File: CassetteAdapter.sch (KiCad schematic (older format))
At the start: 20 parts, among them CN1 AUDIO_IN, CN101 AUDIO_IN_JACK, CN2 TAPE_PORT, SW1 SW_INVERT1, U1 CD4049, U2 LM741

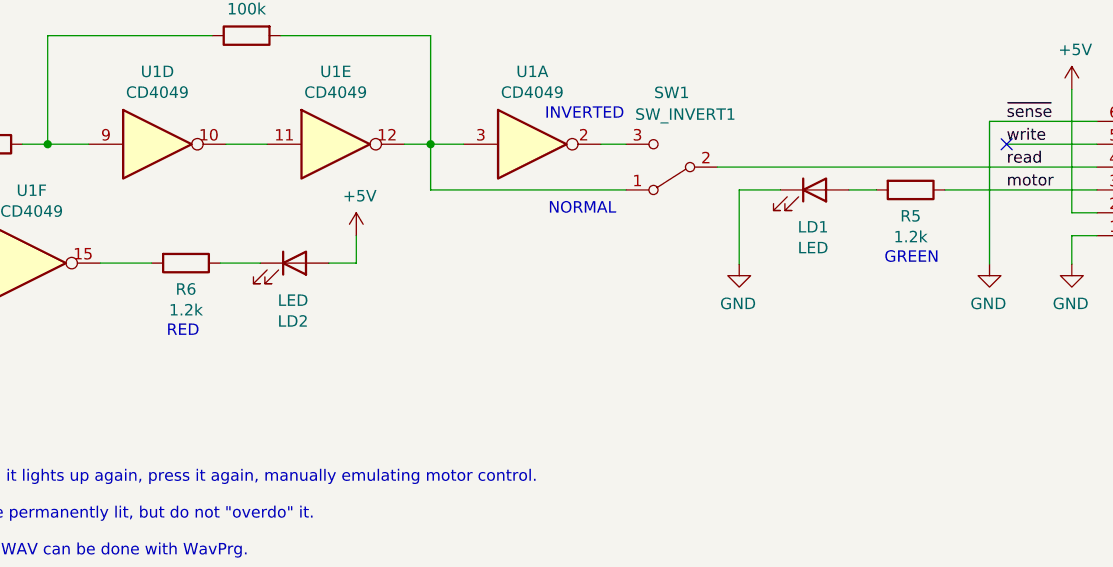
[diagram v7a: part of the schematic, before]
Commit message: LED resistors -> 1k
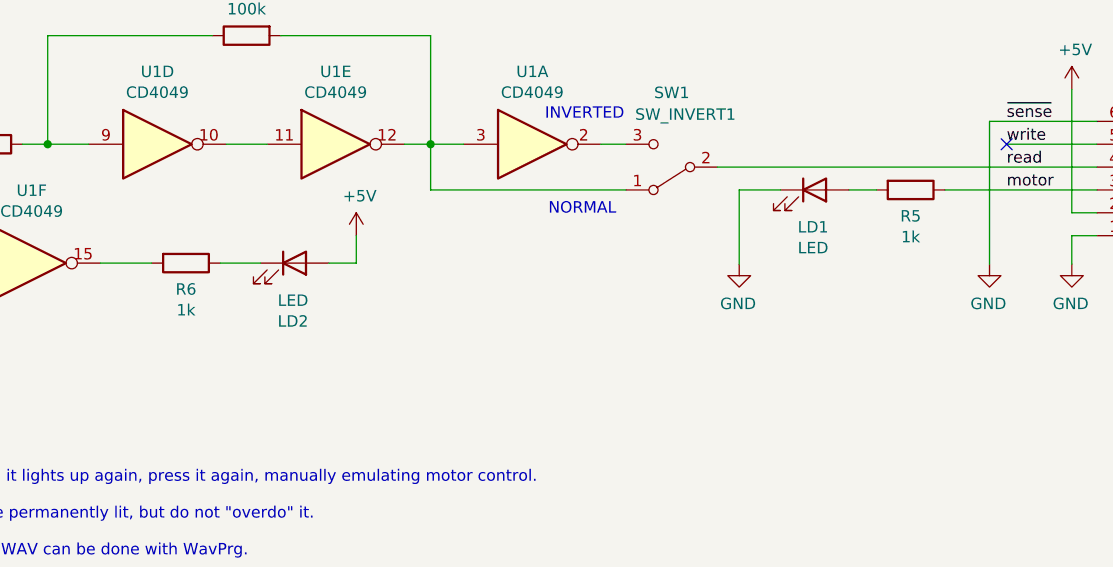
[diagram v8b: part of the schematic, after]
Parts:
- R5, R6: value 1.2k -> 1k
- V0: MouserPN (none) -> ---
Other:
- note removed: "GREEN"
- note removed: "RED"
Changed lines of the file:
@@
 P 9655 2395
 F 0 "R5" V 9770 2395 50  0000 C CNN
-F 1 "1.2k" V 9861 2395 50  0000 C CNN
+F 1 "1k" V 9861 2395 50  0000 C CNN
 F 2 "Resistor_THT:R_Axial_DIN0207_L6.3mm_D2.5mm_P10.16mm_Horizontal" V 9585 2395 50  0001 C CNN
 F 3 "~" H 9655 2395 50  0001 C CNN
@@
 P 6485 2715
 F 0 "R6" V 6600 2715 50  0000 C CNN
-F 1 "1.2k" V 6691 2715 50  0000 C CNN
+F 1 "1k" V 6691 2715 50  0000 C CNN
 F 2 "Resistor_THT:R_Axial_DIN0207_L6.3mm_D2.5mm_P10.16mm_Horizontal" V 6415 2715 50  0001 C CNN
 F 3 "~" H 6485 2715 50  0001 C CNN
@@
 Wire Wire Line
 	1075 6380 1075 6425
-Text Notes 6400 3045 0    50   ~ 0
-RED
-Text Notes 9540 2725 0    50   ~ 0
-GREEN
 $Comp
 L Connector:AudioJack3_SwitchTR CN101
@@
 F 2 "CassetteAdapter:cc_by_nc_sa_small" H 10590 6380 50  0001 C CNN
 F 3 "" H 10590 6380 50  0001 C CNN
+F 4 "---" H 10590 6380 50  0001 C CNN "MouserPN"
 	1    10590 6380
 	1    0    0    -1
@@
 P 7230 2595
 AR Path="/67ABBA81/67EA1CDE" Ref="#PWR?"  Part="1"
-AR Path="/67EA1CDE" Ref="#PWR?"  Part="1"
-F 0 "#PWR?" H 7230 2445 50  0001 C CNN
+AR Path="/67EA1CDE" Ref="#PWR0104"  Part="1"
+F 0 "#PWR0104" H 7230 2445 50  0001 C CNN
 F 1 "+5V" H 7245 2768 50  0000 C CNN
 F 2 "" H 7230 2595 50  0001 C CNN
